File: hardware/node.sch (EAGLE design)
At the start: 48 parts, among them Q1 P-MOSFET, U1 ATMEGA32U4, U2 MCP1703CB/TOREX-XC6206, Y1 8MHz

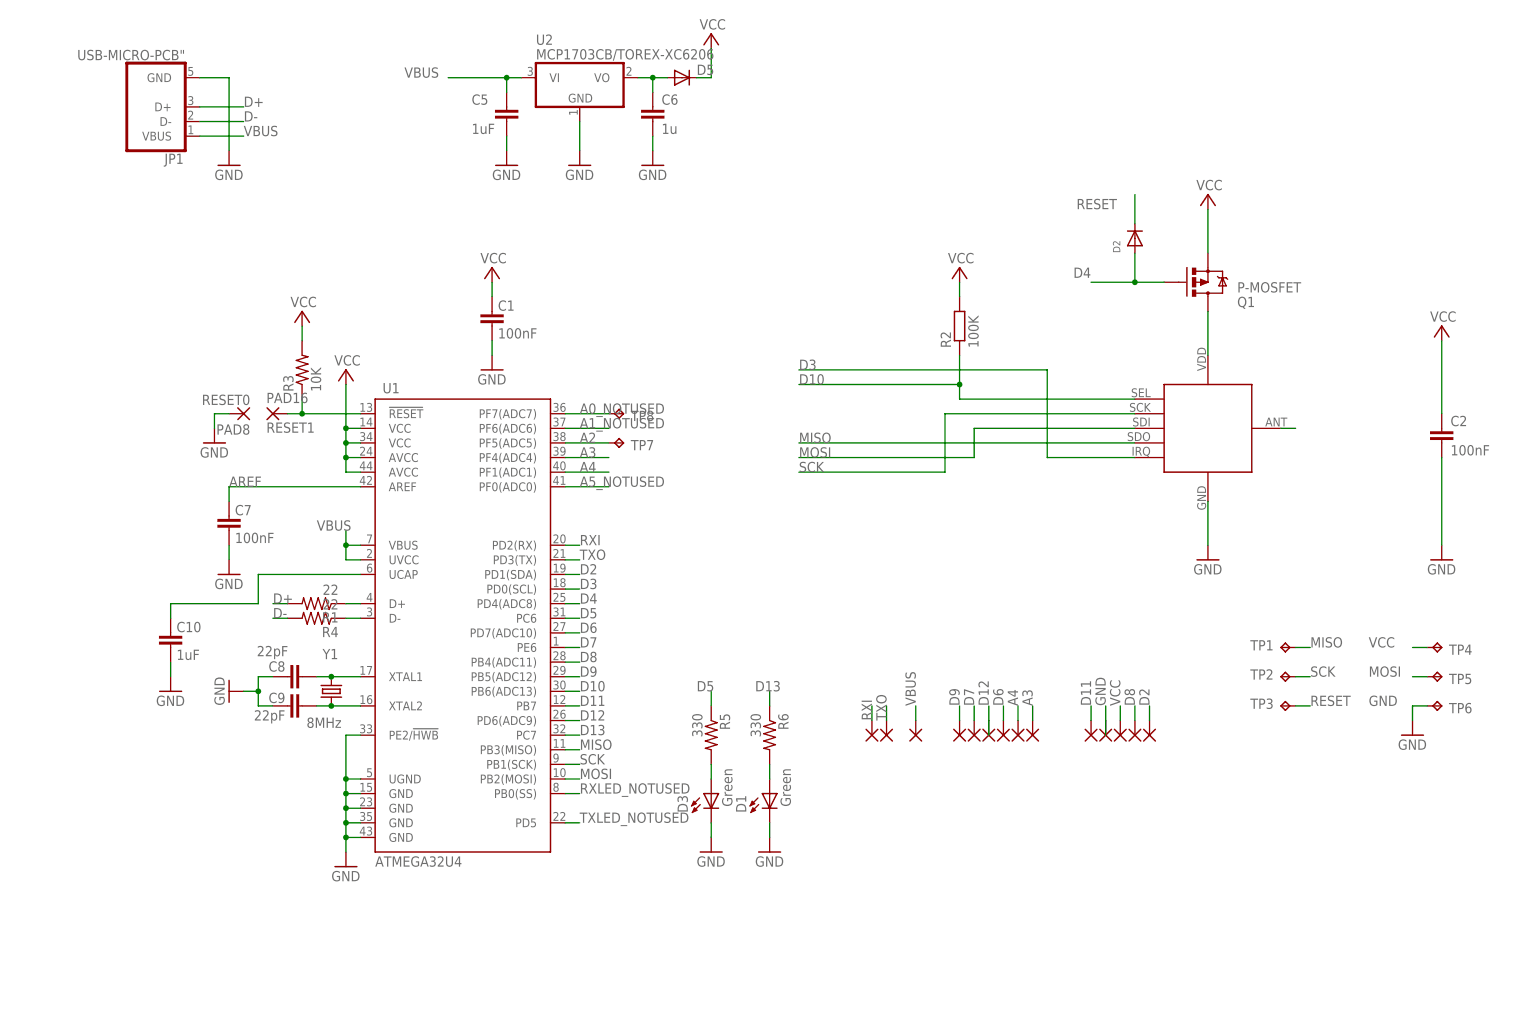
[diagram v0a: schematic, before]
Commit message: Hardware update
Node 1.0.0, export and node shield
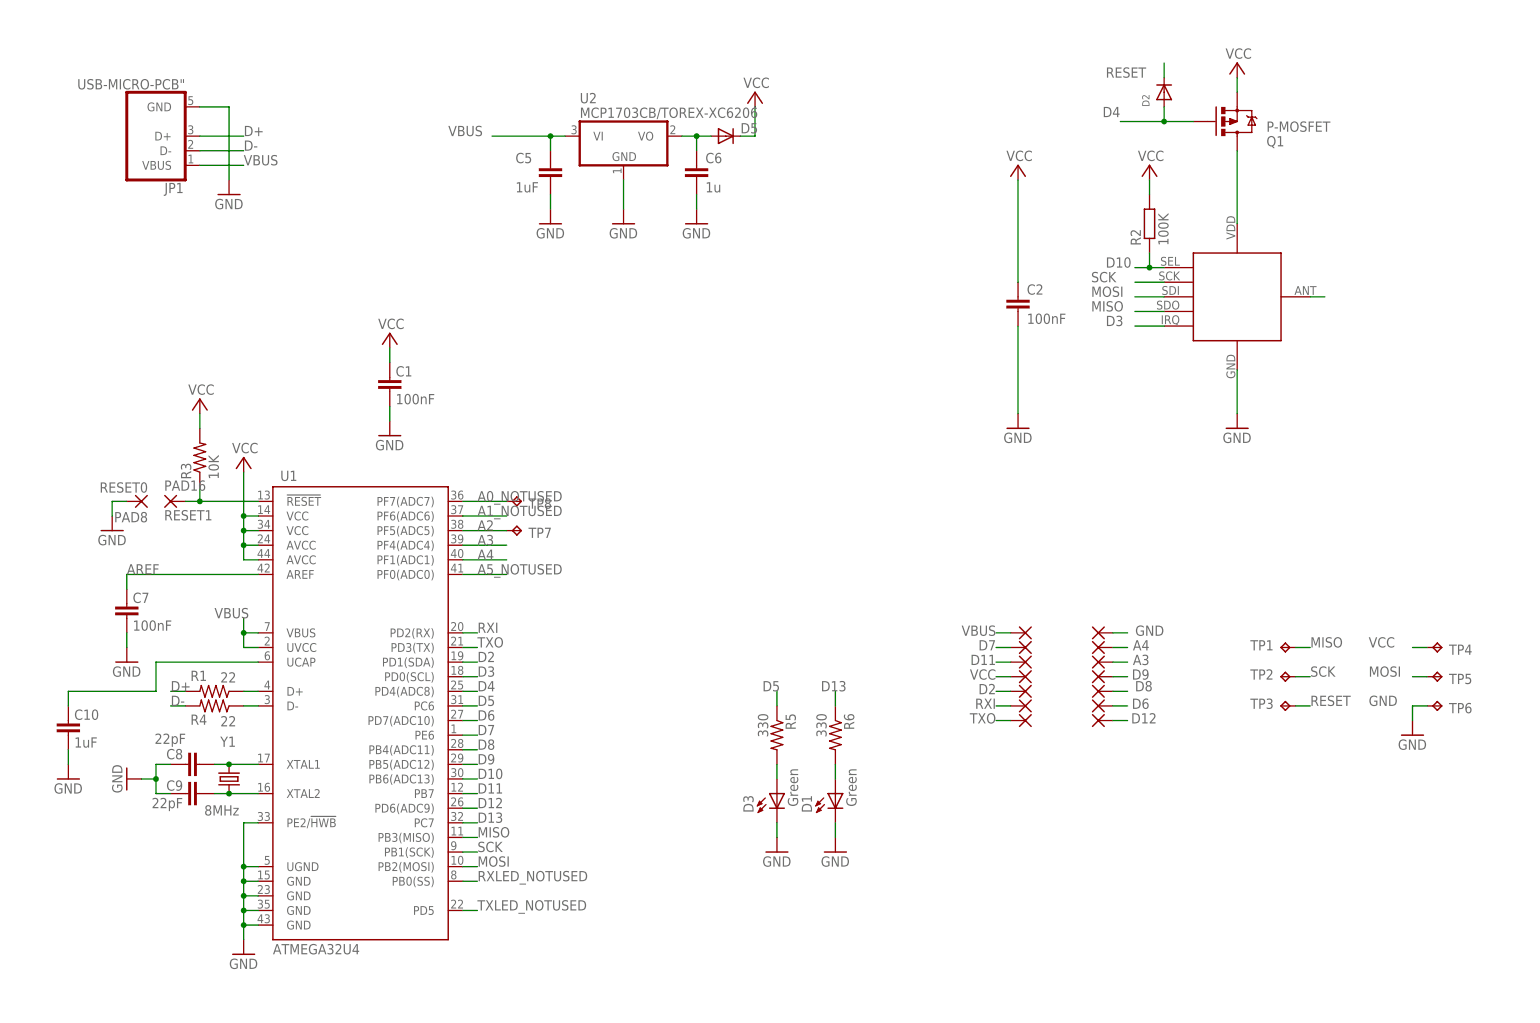
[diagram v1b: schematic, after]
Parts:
- TP1, TP2, TP3, TP4, TP5, TP6: value TPTP08R -> TPTP09R; device testpad:TPTP08R -> testpad:TPTP09R
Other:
- note added: "Interface"
- note added: "Power / USB"
- note added: "RF"
- note added: "µC"
- moved on the sheet: C1, C10, C2, C5, C6, C7, C8, C9, D1, D2, D3, D5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

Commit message: Before resize
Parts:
- added C3, C4: 1uF, SparkFun:CAP0402-CAP
- added IC1: MAX1555, maxim:MAX1555
- added R7, R8: (no value), SparkFun:RESISTOR0402-RES
- added SV1: (no value), con-lsta:FE10-1
- added TP10, TP9: TPTP08R, testpad:TPTP08R
- C2: value 100nF -> 1uF; device rcl:C-EUC0603K -> SparkFun:CAP0402-CAP
- C5: value 1uF -> 100nF; device rcl:C-EUC0603K -> SparkFun:CAP0402-CAP
- C6: value 1u -> 1uF; device rcl:C-EUC0603K -> SparkFun:CAP0402-CAP
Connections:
- net D10 renamed D10_SEL
- net D13 renamed D13_LED_RED
- net D5 renamed D5_LED_GREEN
- net RXI renamed D0
- net TXO renamed D1
- removed net A0_NOTUSED: TP8.TP, U1.PF7(ADC7)
- removed net A1_NOTUSED: U1.PF6(ADC6)
- removed net A5_NOTUSED: U1.PF0(ADC0)
- removed net D11: PAD7.P, U1.PB7
- new net A0: PAD6.P, U1.PF7(ADC7)
- new net A1: PAD5.P, U1.PF6(ADC6)
- new net A5: TP10.TP, U1.PF0(ADC0)
- new net D11_IRQ: RFM12B1.IRQ, U1.PB7
- new net N$28: IC1.!CHG
- new net N$9: C2.2, IC1.USB
- net A3: now also TP8.TP; no longer PAD6.P
- net A4: now also R7.1, R8.2; no longer PAD5.P
- net D3: now also PAD7.P; no longer RFM12B1.IRQ
- net GND: now also C2.1, C3.1, C4.1, C5.1, C6.1, IC1.GND, R8.1; no longer C2.2, C5.2, C6.2
- net N$11: now also C4.2; no longer C6.1
- net TXLED_NOTUSED: now also TP9.TP
- net VBUS: now also C3.2, R7.2; no longer C5.1
- net VCC: now also C5.2, C6.2, IC1.BAT; no longer C2.1
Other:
- note added: "C3, C4, C5 : 0603 -> 0402"
- moved on the sheet: C2, C5, C6, D5, JP1, TP8, U2

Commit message: New node
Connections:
- removed net N$9: C2.2, IC1.USB
- net VBUS: now also C2.2, IC1.USB
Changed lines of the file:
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@@
 <setting verticaltext="up"/>
 </settings>
-<grid distance="0.05" unitdist="inch" unit="inch" style="dots" multiple="1" display="yes" altdistance="0.01" altunitdist="inch" altunit="inch"/>
+<grid distance="0.1" unitdist="inch" unit="inch" style="lines" multiple="1" display="no" altdistance="0.01" altunitdist="inch" altunit="inch"/>
 <layers>
 <layer number="1" name="Top" color="4" fill="1" visible="no" active="no"/>
@@
 <label x="63.5" y="77.47" size="1.778" layer="95" rot="R180"/>
 </segment>
+<segment>
+<pinref part="IC1" gate="G$1" pin="USB"/>
+<wire x1="6.35" y1="106.68" x2="3.81" y2="106.68" width="0.1524" layer="91"/>
+<pinref part="C2" gate="G$1" pin="2"/>
+<wire x1="3.81" y1="104.14" x2="3.81" y2="106.68" width="0.1524" layer="91"/>
+<wire x1="3.81" y1="106.68" x2="1.27" y2="106.68" width="0.1524" layer="91"/>
+<junction x="3.81" y="106.68"/>
+<label x="-7.62" y="106.68" size="1.778" layer="95"/>
+</segment>
 </net>
 <net name="D+" class="0">
@@
 </segment>
 </net>
-<net name="N$9" class="0">
-<segment>
-<pinref part="IC1" gate="G$1" pin="USB"/>
-<wire x1="6.35" y1="106.68" x2="3.81" y2="106.68" width="0.1524" layer="91"/>
-<pinref part="C2" gate="G$1" pin="2"/>
-<wire x1="3.81" y1="104.14" x2="3.81" y2="106.68" width="0.1524" layer="91"/>
-<wire x1="3.81" y1="106.68" x2="1.27" y2="106.68" width="0.1524" layer="91"/>
-<junction x="3.81" y="106.68"/>
-</segment>
-</net>

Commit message: Node
Avancement
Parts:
- added PAD17, PAD18, PAD19, PAD20, PAD21, PAD22, PAD23, PAD24, PAD25, PAD26, PAD27, PAD28, PAD29, PAD30, PAD31, PAD32, PAD33, PAD34, PAD35, PAD36, PAD37, PAD38, PAD39, PAD40, PAD41, PAD42, PAD43, PAD44, PAD45, PAD46, PAD47, PAD48, PAD49, PAD50, PAD51, PAD52, PAD53, PAD54, PAD55, PAD56, PAD57, PAD58: (no value), wirepad:SMD2
- added TP11: TPTP08R, testpad:TPTP08R
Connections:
- net TXLED_NOTUSED renamed TXLED
- removed net RXLED_NOTUSED: U1.PB0(SS)
- new net N$13: PAD33.P, PAD34.P
- new net N$27: PAD35.P, PAD36.P
- new net N$29: PAD37.P, PAD38.P
- new net N$30: PAD39.P, PAD40.P
- new net N$31: PAD41.P, PAD42.P
- new net N$32: PAD43.P, PAD44.P
- new net N$40: PAD45.P, PAD46.P
- new net N$41: PAD47.P, PAD48.P
- new net N$42: PAD49.P, PAD50.P
- new net N$43: PAD51.P, PAD52.P
- new net N$44: PAD53.P, PAD54.P
- new net N$45: PAD55.P, PAD56.P
- new net N$46: PAD57.P, PAD58.P
- new net N$9: PAD31.P, PAD32.P
- new net RXLED: TP11.TP, U1.PB0(SS)
- net A0: now also PAD29.P
- net A1: now also PAD30.P
- net D0: now also PAD23.P
- net D1: now also PAD22.P
- net D12: now also PAD28.P
- net D2: now also PAD21.P
- net D3: now also PAD20.P
- net D6: now also PAD24.P
- net D7: now also PAD25.P
- net D8: now also PAD26.P
- net D9: now also PAD27.P
- net GND: now also PAD18.P
- net VBUS: now also PAD17.P
- net VCC: now also PAD19.P
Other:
- note added: "INT: D0, D1, D2, D3, D7"
- note added: "PCINT: D8, D9"
- moved on the sheet: TP9

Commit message: Node
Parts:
- removed SV1: (no value), con-lsta:FE10-1
- added TP12: TPTP08R, testpad:TPTP08R
- D5: value (none) -> RB751S40
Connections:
- net VBUS renamed VIN
- removed net N$28: IC1.!CHG
- new net CHG: IC1.!CHG, TP12.TP, U1.PE2/!HWB
- net GND: no longer U1.PE2/!HWB
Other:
- note added: "Shield"
- moved on the sheet: C10, C7, D1, D2, D3, R5, R6, R7, R8

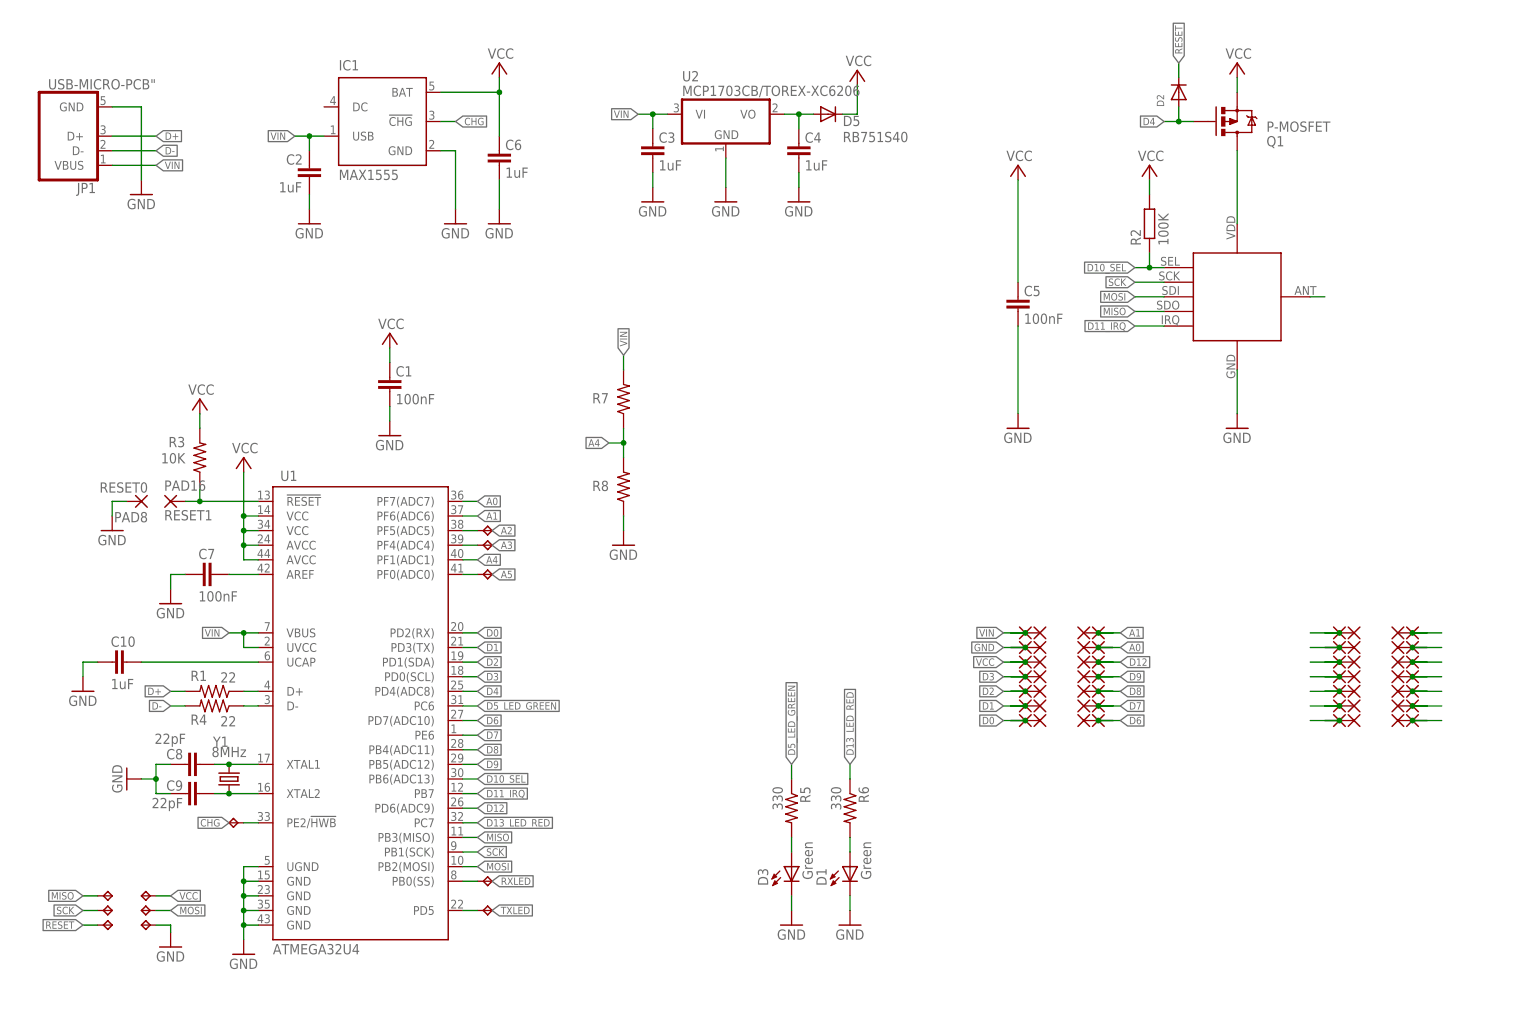
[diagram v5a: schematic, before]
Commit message: Max1555 backup
Finally, design with max1555 is a bad idea !
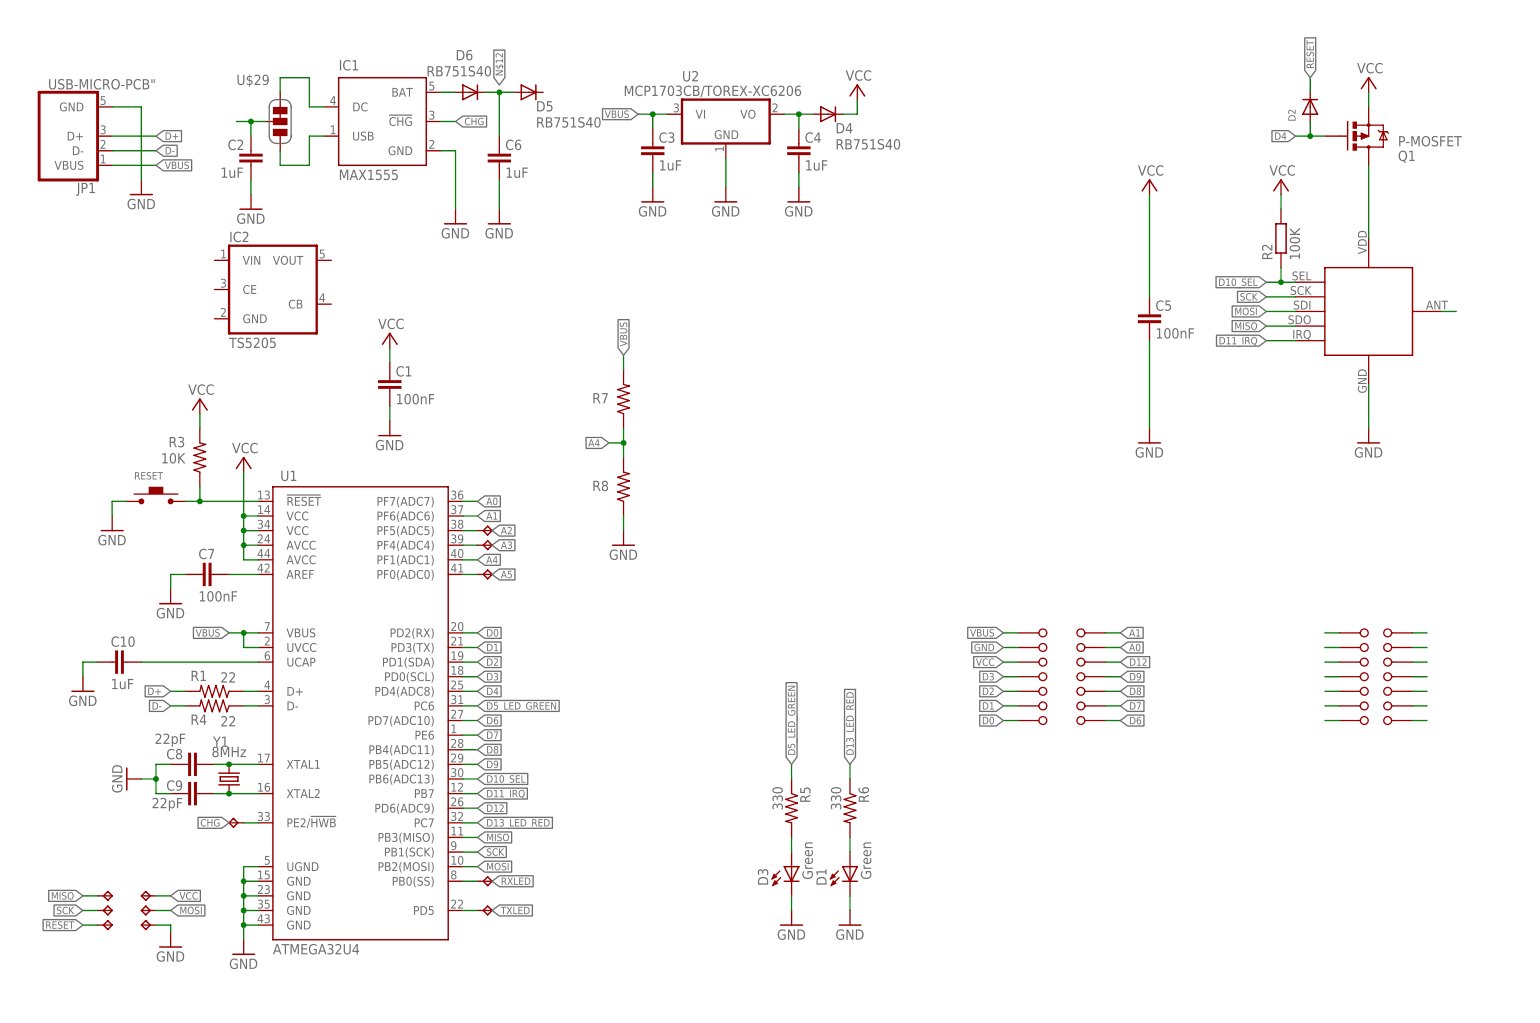
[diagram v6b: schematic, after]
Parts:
- removed PAD1, PAD10, PAD11, PAD12, PAD13, PAD14, PAD15, PAD17, PAD18, PAD19, PAD2, PAD20, PAD21, PAD22, PAD23, PAD24, PAD25, PAD26, PAD27, PAD28, PAD29, PAD3, PAD30, PAD31, PAD32, PAD33, PAD34, PAD35, PAD36, PAD37, PAD38, PAD39, PAD4, PAD40, PAD41, PAD42, PAD43, PAD44, PAD45, PAD46, PAD47, PAD48, PAD49, PAD5, PAD50, PAD51, PAD52, PAD53, PAD54, PAD55, PAD56, PAD57, PAD58, PAD6, PAD7, PAD9: (no value), wirepad:SMD2
- removed PAD16: RESET1, wirepad:WIREPADSMD1,27-254
- removed PAD8: RESET0, wirepad:WIREPADSMD1,27-254
- removed RFM12B1: RFM12B_MINPADS, LowPowerLab:RFM12B_MINPADS
- removed TP6: TPTP09R, testpad:TPTP09R
- added D4, D6: RB751S40, diode:DIODE-SOD523
- added IC2: TS5205, v-reg:TS5205
- added RESET: MICROSWITCH, openalarm:MICROSWITCH
- added RFMXX: RFM12B_MINPADS, LowPowerLab:RFM12B_MINPADS
- added TP14: TPTP13R, testpad:TPTP13R
- added U$1, U$10, U$11, U$12, U$13, U$14, U$15, U$16, U$17, U$18, U$19, U$2, U$20, U$21, U$22, U$23, U$24, U$25, U$26, U$27, U$28, U$3, U$4, U$5, U$6, U$7, U$8, U$9: IOPAD, openalarm:IOPAD
- added U$29: UJUMPER-SHORT, openalarm:UJUMPER-SHORT
- TP1, TP2, TP3, TP4, TP5: value TPTP09R -> TPTP13R; device testpad:TPTP09R -> testpad:TPTP13R
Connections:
- removed net VIN: C2.2, C3.2, IC1.USB, JP1.VBUS, PAD15.P, PAD17.P, R7.2, U1.UVCC, U1.VBUS, U2.VI
- new net N$12: C6.2, D5.A, D6.C
- new net N$14: IC1.DC, U$29.C0
- new net N$15: C2.2, U$29.COM
- new net N$16: D6.A, IC1.BAT
- new net VBAT: C4.2, D4.A, U2.VO
- new net VBUS: C3.2, JP1.VBUS, R7.2, U$7.P$1, U1.UVCC, U1.VBUS, U2.VI
- net A0: now also U$9.P$1; no longer PAD29.P, PAD6.P
- net A1: now also U$8.P$1; no longer PAD30.P, PAD5.P
- net D0: now also U$2.P$1; no longer PAD14.P, PAD23.P
- net D1: now also U$1.P$1; no longer PAD13.P, PAD22.P
- net D10_SEL: now also RFMXX.SEL; no longer RFM12B1.SEL
- net D11_IRQ: now also RFMXX.IRQ; no longer RFM12B1.IRQ
- net D12: now also U$10.P$1; no longer PAD28.P, PAD3.P
- net D2: now also U$3.P$1; no longer PAD12.P, PAD21.P
- net D3: now also U$4.P$1; no longer PAD20.P, PAD7.P
- net D6: now also U$14.P$1; no longer PAD24.P, PAD4.P
- net D7: now also U$13.P$1; no longer PAD2.P, PAD25.P
- net D8: now also U$12.P$1; no longer PAD11.P, PAD26.P
- net D9: now also U$11.P$1; no longer PAD1.P, PAD27.P
- net GND: now also RESET.P$1, RFMXX.GND, TP5.TP, U$6.P$1; no longer PAD18.P, PAD8.P, PAD9.P, RFM12B1.GND, TP6.TP
- net MISO: now also RFMXX.SDO/MISO, TP14.TP; no longer RFM12B1.SDO/MISO, TP1.TP
- net MOSI: now also RFMXX.SDI/MOSI, TP4.TP; no longer RFM12B1.SDI/MOSI, TP5.TP
- net N$10: now also RFMXX.VDD; no longer RFM12B1.VDD
- net N$11: now also IC1.USB, U$29.C1; no longer C4.2, D5.A, U2.VO
- net N$13: now also U$16.P$1; no longer PAD33.P, PAD34.P
- net N$27: now also U$17.P$1; no longer PAD35.P, PAD36.P
- net N$29: now also U$18.P$1; no longer PAD37.P, PAD38.P
- net N$3: now also RFMXX.ANT; no longer RFM12B1.ANT
- net N$30: now also U$19.P$1; no longer PAD39.P, PAD40.P
- net N$31: now also U$20.P$1; no longer PAD41.P, PAD42.P
- net N$32: now also U$21.P$1; no longer PAD43.P, PAD44.P
- net N$40: now also U$23.P$1; no longer PAD45.P, PAD46.P
- net N$41: now also U$24.P$1; no longer PAD47.P, PAD48.P
- net N$42: now also U$25.P$1; no longer PAD49.P, PAD50.P
- net N$43: now also U$26.P$1; no longer PAD51.P, PAD52.P
- net N$44: now also U$27.P$1; no longer PAD53.P, PAD54.P
- net N$45: now also U$28.P$1; no longer PAD55.P, PAD56.P
- net N$46: now also U$22.P$1; no longer PAD57.P, PAD58.P
- net N$9: now also U$15.P$1; no longer PAD31.P, PAD32.P
- net RESET: now also RESET.P$2; no longer PAD16.P
- net SCK: now also RFMXX.SCK; no longer RFM12B1.SCK
- net VCC: now also D4.C, TP1.TP, U$5.P$1; no longer C6.2, D5.C, IC1.BAT, PAD10.P, PAD19.P, TP4.TP
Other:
- moved on the sheet: C2, C5, D2, D5, Q1, R2
